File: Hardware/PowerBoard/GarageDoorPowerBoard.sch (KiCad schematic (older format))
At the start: 10 parts, among them J1 1984617, J2 Conn_01x06, J3 RJ45

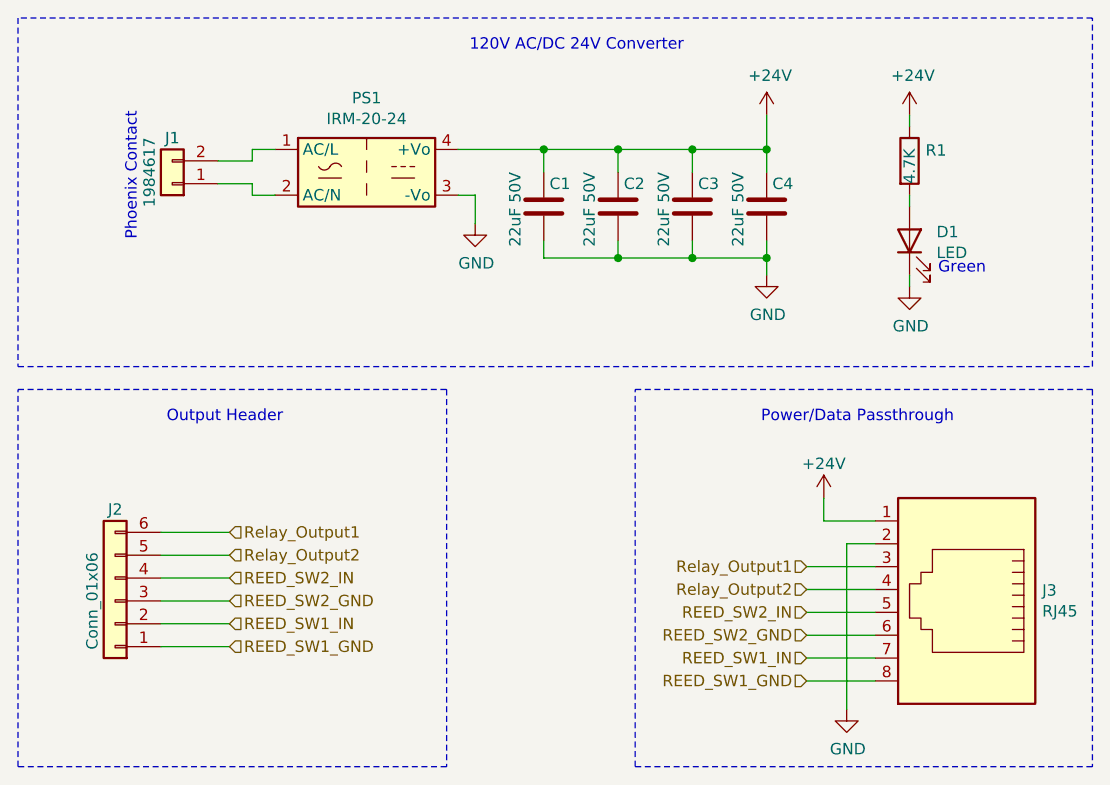
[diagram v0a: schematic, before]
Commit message: Schematics done, PCBs have components dropped in and BoM finished
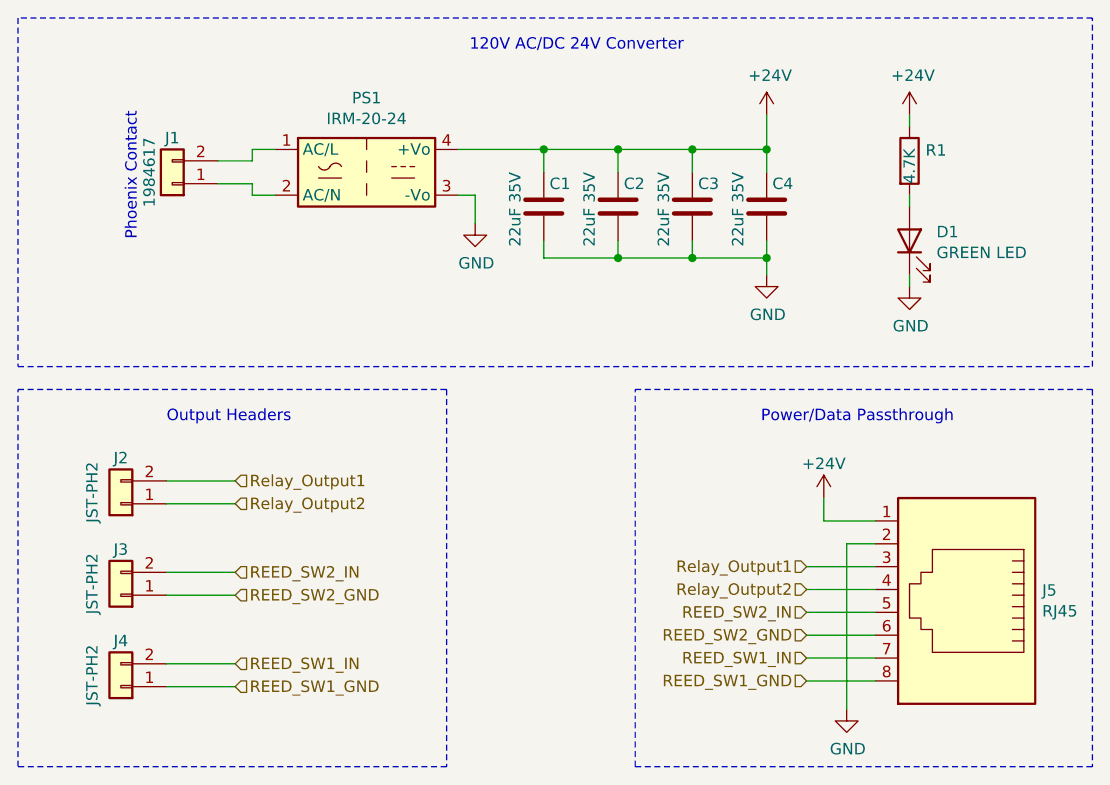
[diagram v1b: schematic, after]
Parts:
- removed J2: Conn_01x06, symbol conn:Conn_01x06
- added J2, J3, J4: JST-PH2, Connector_JST:JST_PH_S2B-PH-K_1x02_P2.00mm_Horizontal, symbol conn:Conn_01x02
- C1, C2, C3, C4: value 22uF 50V -> 22uF 35V; footprint (none) -> Capacitor_SMD:C_1206_3216Metric
- D1: value LED -> GREEN LED; footprint (none) -> LED_SMD:LED_0805_2012Metric
- J5: renamed from J3; footprint (none) -> Connector_RJ:RJ45_Amphenol_54602-x08_Horizontal
- R1: footprint (none) -> Resistor_SMD:R_0603_1608Metric
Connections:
- net REED_SW1_GND: now also J4.1 (Pin_1)
- net REED_SW1_IN: now also J4.2 (Pin_2)
- net REED_SW2_GND: now also J3.1 (Pin_1)
- net REED_SW2_IN: now also J3.2 (Pin_2)
- net Relay_Output1: now also J2.2 (Pin_2)
- net Relay_Output2: now also J2.1 (Pin_1)
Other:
- note added: "Output Headers"
- note removed: "Green"
- note removed: "Output Header"
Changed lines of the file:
@@
 Phoenix Contact
 $Comp
-L Connector:RJ45 J3
+L Connector:RJ45 J5
 U 1 1 5EAF7510
 P 7525 4650
-F 0 "J3" H 7195 4654 50  0000 R CNN
+F 0 "J5" H 7195 4654 50  0000 R CNN
 F 1 "RJ45" H 7195 4745 50  0000 R CNN
-F 2 "" V 7525 4675 50  0001 C CNN
+F 2 "Connector_RJ:RJ45_Amphenol_54602-x08_Horizontal" V 7525 4675 50  0001 C CNN
 F 3 "~" V 7525 4675 50  0001 C CNN
 	1    7525 4650
@@
 P 5675 2975
 F 0 "C1" H 5700 3075 50  0000 L CNN
-F 1 "22uF 50V" V 5550 2800 50  0000 L CNN
-F 2 "" H 5713 2825 50  0001 C CNN
+F 1 "22uF 35V" V 5550 2800 50  0000 L CNN
+F 2 "Capacitor_SMD:C_1206_3216Metric" H 5713 2825 50  0001 C CNN
 F 3 "~" H 5675 2975 50  0001 C CNN
 	1    5675 2975
@@
 P 6000 2975
 F 0 "C2" H 6025 3075 50  0000 L CNN
-F 1 "22uF 50V" V 5875 2800 50  0000 L CNN
-F 2 "" H 6038 2825 50  0001 C CNN
+F 1 "22uF 35V" V 5875 2800 50  0000 L CNN
+F 2 "Capacitor_SMD:C_1206_3216Metric" H 6038 2825 50  0001 C CNN
 F 3 "~" H 6000 2975 50  0001 C CNN
 	1    6000 2975
@@
 P 6325 2975
 F 0 "C3" H 6350 3075 50  0000 L CNN
-F 1 "22uF 50V" V 6200 2800 50  0000 L CNN
-F 2 "" H 6363 2825 50  0001 C CNN
+F 1 "22uF 35V" V 6200 2800 50  0000 L CNN
+F 2 "Capacitor_SMD:C_1206_3216Metric" H 6363 2825 50  0001 C CNN
 F 3 "~" H 6325 2975 50  0001 C CNN
 	1    6325 2975
@@
 P 6650 2975
 F 0 "C4" H 6675 3075 50  0000 L CNN
-F 1 "22uF 50V" V 6525 2800 50  0000 L CNN
-F 2 "" H 6688 2825 50  0001 C CNN
+F 1 "22uF 35V" V 6525 2800 50  0000 L CNN
+F 2 "Capacitor_SMD:C_1206_3216Metric" H 6688 2825 50  0001 C CNN
 F 3 "~" H 6650 2975 50  0001 C CNN
 	1    6650 2975
@@
 Wire Wire Line
 	5675 2725 6000 2725
-$Comp
-L conn:Conn_01x06 J2
-U 1 1 5EB12C73
-P 3800 4700
-F 0 "J2" H 3800 4300 50  0000 C CNN
-F 1 "Conn_01x06" V 3900 4700 50  0000 C CNN
-F 2 "" H 3800 4700 50  0001 C CNN
-F 3 "~" H 3800 4700 50  0001 C CNN
-	1    3800 4700
-	-1   0    0    1
-$EndComp
-Text HLabel 4300 4400 2    50   Input ~ 0
+Text HLabel 4325 4175 2    50   Input ~ 0
 Relay_Output1
-Text HLabel 4300 4500 2    50   Input ~ 0
+Text HLabel 4325 4275 2    50   Input ~ 0
 Relay_Output2
-Text HLabel 4300 4600 2    50   Input ~ 0
+Text HLabel 4325 4575 2    50   Input ~ 0
 REED_SW2_IN
 Wire Wire Line
-	4300 4600 4000 4600
-Wire Wire Line
-	4000 4500 4300 4500
-Wire Wire Line
-	4300 4400 4000 4400
-Text HLabel 4300 4800 2    50   Input ~ 0
+	4325 4575 4025 4575
+Wire Wire Line
+	4025 4275 4325 4275
+Wire Wire Line
+	4325 4175 4025 4175
+Text HLabel 4325 4975 2    50   Input ~ 0
 REED_SW1_IN
-Text HLabel 4300 4700 2    50   Input ~ 0
+Text HLabel 4325 4675 2    50   Input ~ 0
 REED_SW2_GND
-Text HLabel 4300 4900 2    50   Input ~ 0
+Text HLabel 4325 5075 2    50   Input ~ 0
 REED_SW1_GND
 Wire Wire Line
-	4300 4900 4000 4900
-Wire Wire Line
-	4000 4800 4300 4800
-Wire Wire Line
-	4300 4700 4000 4700
+	4325 5075 4025 5075
+Wire Wire Line
+	4025 4975 4325 4975
+Wire Wire Line
+	4325 4675 4025 4675
 $Comp
 L power:+24V #PWR06
@@
 F 0 "R1" H 7345 2821 50  0000 L CNN
 F 1 "4.7K" V 7275 2675 50  0000 L CNN
-F 2 "" V 7205 2775 50  0001 C CNN
+F 2 "Resistor_SMD:R_0603_1608Metric" V 7205 2775 50  0001 C CNN
 F 3 "~" H 7275 2775 50  0001 C CNN
 	1    7275 2775
@@
 P 7275 3125
 F 0 "D1" V 7314 3007 50  0000 R CNN
-F 1 "LED" V 7223 3007 50  0000 R CNN
-F 2 "" H 7275 3125 50  0001 C CNN
+F 1 "GREEN LED" V 7223 3007 50  0000 R CNN
+F 2 "LED_SMD:LED_0805_2012Metric" H 7275 3125 50  0001 C CNN
 F 3 "~" H 7275 3125 50  0001 C CNN
 	1    7275 3125
@@
 Wire Wire Line
 	7275 2575 7275 2625
-Text Notes 7400 3275 0    50   ~ 0
-Green
 Wire Notes Line
 	3375 3675 8075 3675
@@
 	3375 3775 5250 3775
 Text Notes 4025 3925 0    50   ~ 0
-Output Header
+Output Headers
 Text Notes 6625 3925 0    50   ~ 0
 Power/Data Passthrough
+$Comp
+L conn:Conn_01x02 J3
+U 1 1 5EB0B896
+P 3825 4675
+F 0 "J3" H 3825 4475 50  0000 C CNN
+F 1 "JST-PH2" V 3950 4625 50  0000 C CNN
+F 2 "Connector_JST:JST_PH_S2B-PH-K_1x02_P2.00mm_Horizontal" H 3825 4675 50  0001 C CNN
+F 3 "~" H 3825 4675 50  0001 C CNN
+	1    3825 4675
+	-1   0    0    1
+$EndComp
+$Comp
+L conn:Conn_01x02 J2
+U 1 1 5EB0C691
+P 3825 4275
+F 0 "J2" H 3825 4075 50  0000 C CNN
+F 1 "JST-PH2" V 3950 4225 50  0000 C CNN
+F 2 "Connector_JST:JST_PH_S2B-PH-K_1x02_P2.00mm_Horizontal" H 3825 4275 50  0001 C CNN
+F 3 "~" H 3825 4275 50  0001 C CNN
+	1    3825 4275
+	-1   0    0    1
+$EndComp
+$Comp
+L conn:Conn_01x02 J4
+U 1 1 5EB0E3B4
+P 3825 5075
+F 0 "J4" H 3825 4875 50  0000 C CNN
+F 1 "JST-PH2" V 3950 5025 50  0000 C CNN
+F 2 "Connector_JST:JST_PH_S2B-PH-K_1x02_P2.00mm_Horizontal" H 3825 5075 50  0001 C CNN
+F 3 "~" H 3825 5075 50  0001 C CNN
+	1    3825 5075
+	-1   0    0    1
+$EndComp
 $EndSCHEMATC

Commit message: started work on the power PCB, board shape and basic placement complete
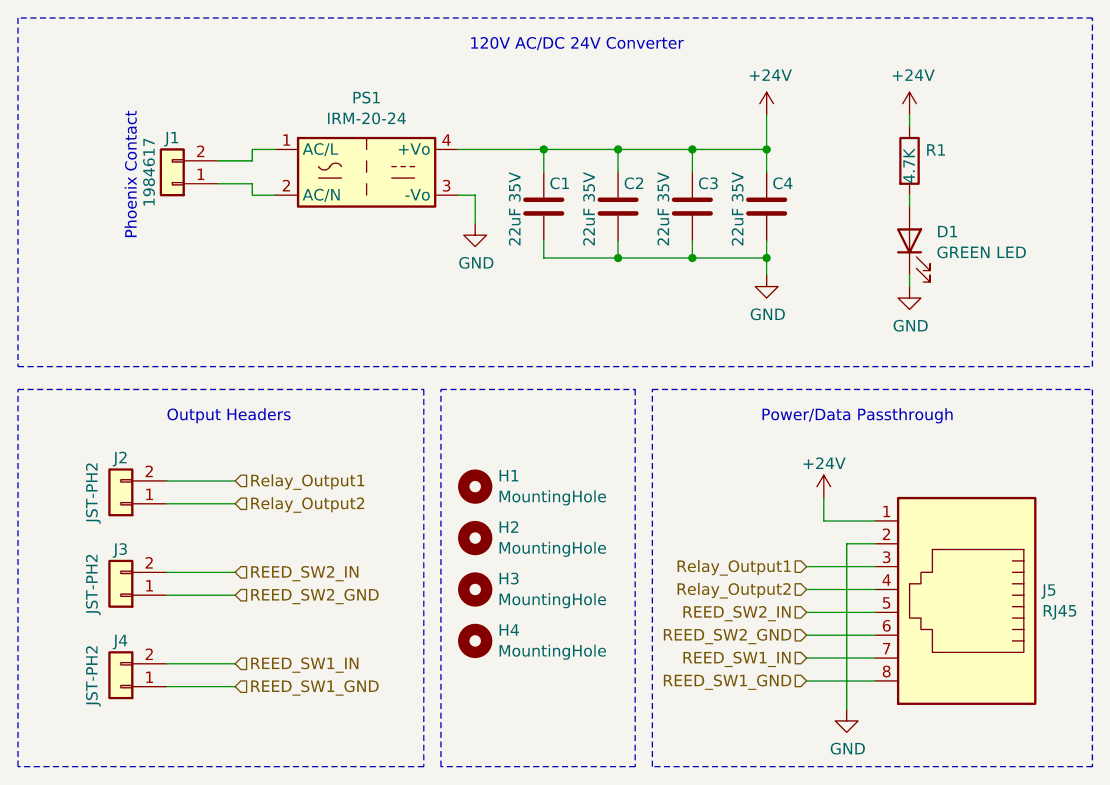
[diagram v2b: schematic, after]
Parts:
- added H1, H2, H3, H4: MountingHole, MountingHole:MountingHole_3.2mm_M3, symbol mechanical:MountingHole
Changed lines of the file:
@@
 	8075 3775 8075 5425
 Wire Notes Line
-	8075 5425 6075 5425
+	8075 5425 6150 5425
 Wire Notes Line
-	6075 5425 6075 3775
+	6150 5425 6150 3775
 Wire Notes Line
-	6075 3775 8075 3775
+	6150 3775 8075 3775
 Wire Notes Line
-	5250 3775 5250 5425
+	5150 3775 5150 5425
 Wire Notes Line
-	5250 5425 3375 5425
+	5150 5425 3375 5425
 Wire Notes Line
 	3375 5425 3375 3775
 Wire Notes Line
-	3375 3775 5250 3775
+	3375 3775 5150 3775
 Text Notes 4025 3925 0    50   ~ 0
 Output Headers
@@
 	-1   0    0    1
 $EndComp
+$Comp
+L mechanical:MountingHole H1
+U 1 1 5EB4431A
+P 5375 4200
+F 0 "H1" H 5475 4246 50  0000 L CNN
+F 1 "MountingHole" H 5475 4155 50  0000 L CNN
+F 2 "MountingHole:MountingHole_3.2mm_M3" H 5375 4200 50  0001 C CNN
+F 3 "~" H 5375 4200 50  0001 C CNN
+	1    5375 4200
+	1    0    0    -1
+$EndComp
+$Comp
+L mechanical:MountingHole H2
+U 1 1 5EB44A92
+P 5375 4425
+F 0 "H2" H 5475 4471 50  0000 L CNN
+F 1 "MountingHole" H 5475 4380 50  0000 L CNN
+F 2 "MountingHole:MountingHole_3.2mm_M3" H 5375 4425 50  0001 C CNN
+F 3 "~" H 5375 4425 50  0001 C CNN
+	1    5375 4425
+	1    0    0    -1
+$EndComp
+$Comp
+L mechanical:MountingHole H3
+U 1 1 5EB44CBA
+P 5375 4650
+F 0 "H3" H 5475 4696 50  0000 L CNN
+F 1 "MountingHole" H 5475 4605 50  0000 L CNN
+F 2 "MountingHole:MountingHole_3.2mm_M3" H 5375 4650 50  0001 C CNN
+F 3 "~" H 5375 4650 50  0001 C CNN
+	1    5375 4650
+	1    0    0    -1
+$EndComp
+$Comp
+L mechanical:MountingHole H4
+U 1 1 5EB45056
+P 5375 4875
+F 0 "H4" H 5475 4921 50  0000 L CNN
+F 1 "MountingHole" H 5475 4830 50  0000 L CNN
+F 2 "MountingHole:MountingHole_3.2mm_M3" H 5375 4875 50  0001 C CNN
+F 3 "~" H 5375 4875 50  0001 C CNN
+	1    5375 4875
+	1    0    0    -1
+$EndComp
+Wire Notes Line
+	6075 3775 6075 5425
+Wire Notes Line
+	6075 5425 5225 5425
+Wire Notes Line
+	5225 5425 5225 3775
+Wire Notes Line
+	5225 3775 6075 3775
 $EndSCHEMATC
